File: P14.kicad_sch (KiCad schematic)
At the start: 12 parts

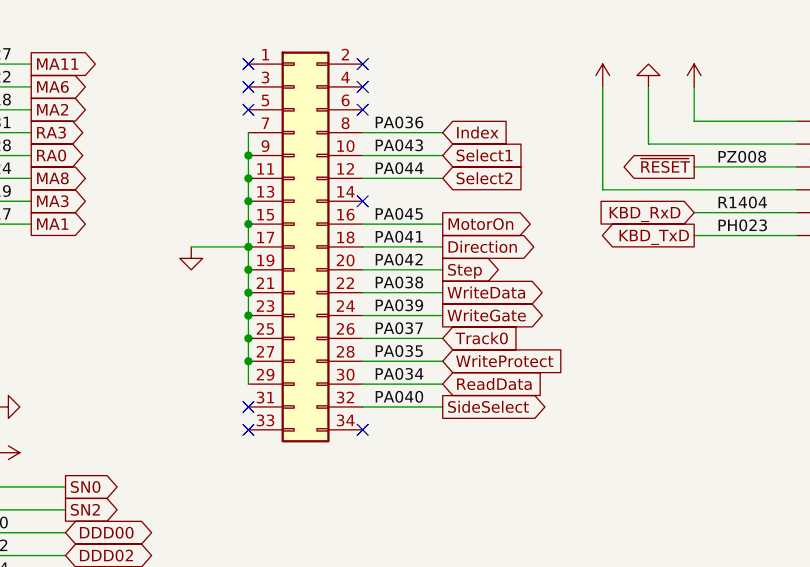
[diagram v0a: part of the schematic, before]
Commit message: fixing KiCad6 warnings
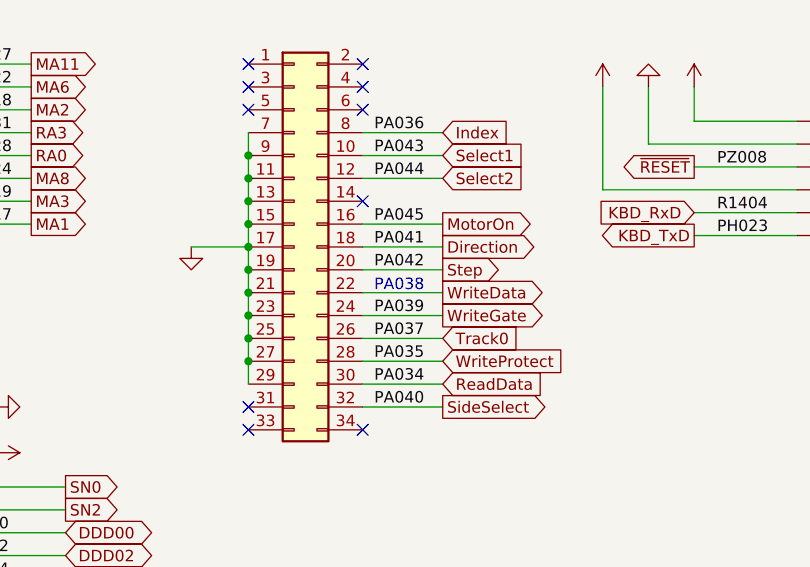
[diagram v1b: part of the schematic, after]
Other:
- note added: "PA038"
